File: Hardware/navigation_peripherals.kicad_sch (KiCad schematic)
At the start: 29 parts, among them J2 5-1814832-1, J3 Conn_01x04, J4 Conn_01x04, U10 BMP390, U11 W25N01GVZEIG_TR, U5 IST8310, U6 NEO-M8N, U7 BMI088, U8 TMP100, U9 24CW1280T-I/OT

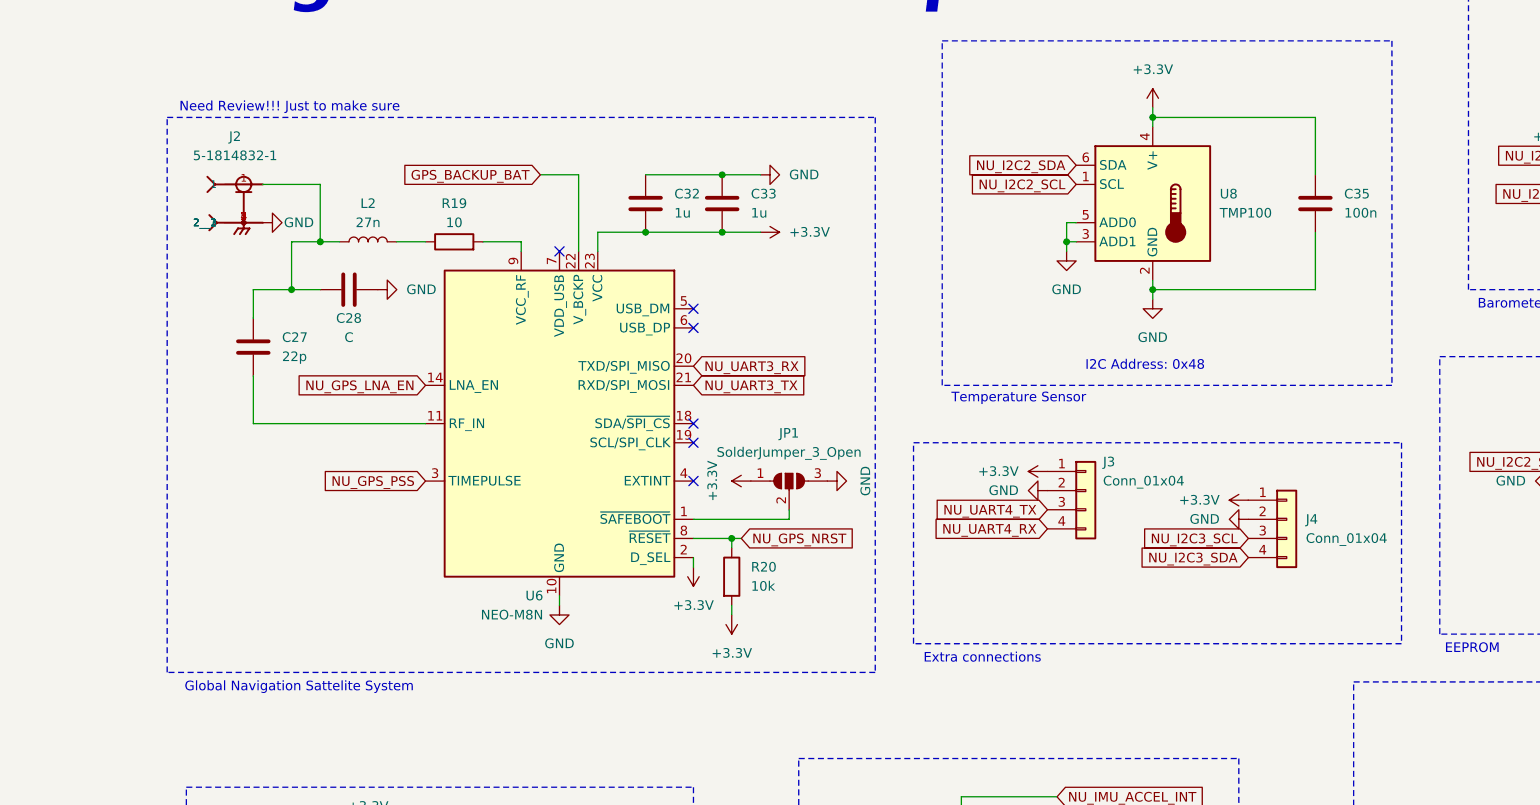
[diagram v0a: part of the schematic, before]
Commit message: hardware version 0.1.2, minor improvements and footprint selection (missing some gnss and bulk regulator components
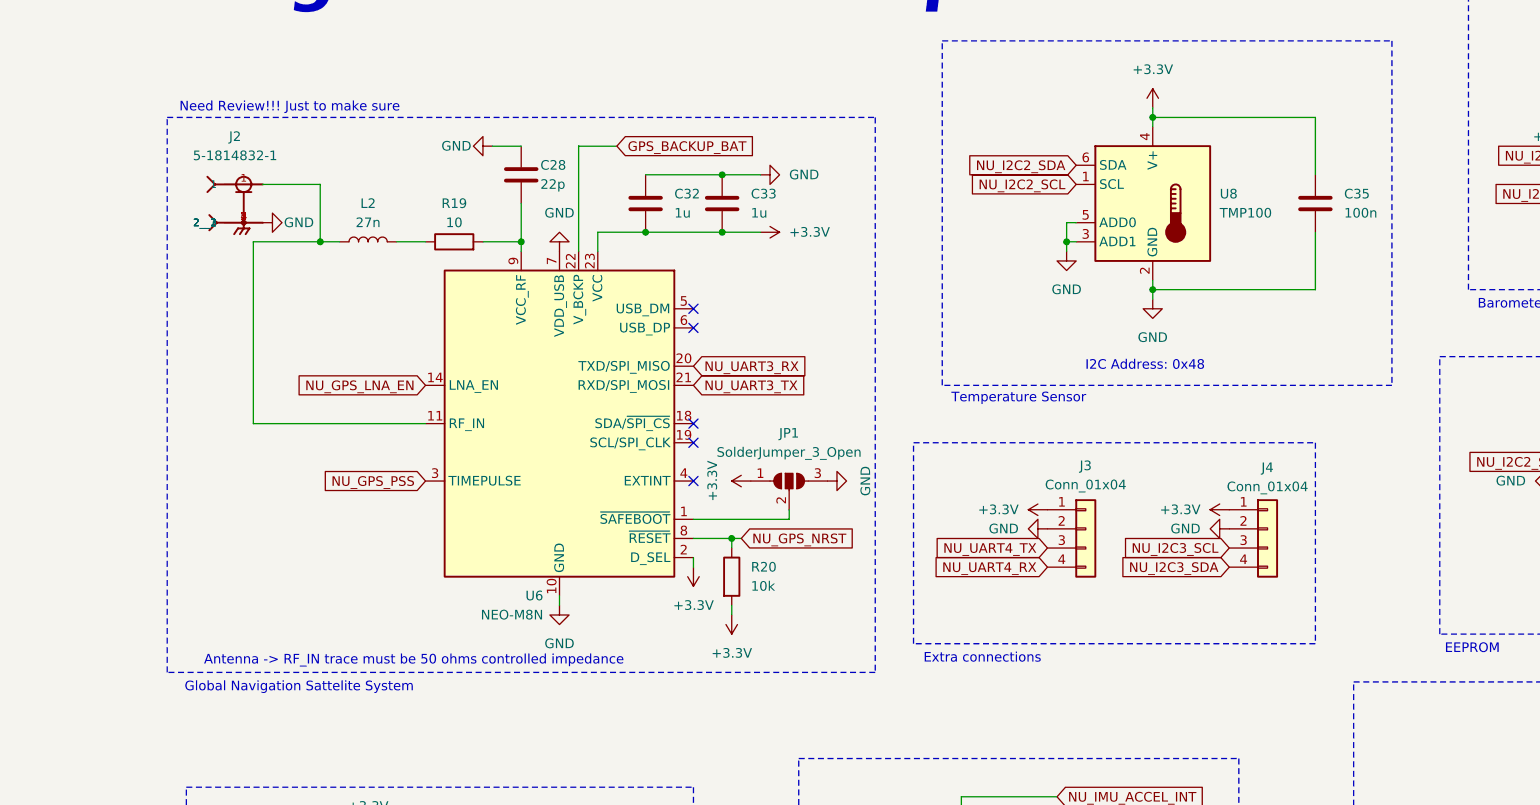
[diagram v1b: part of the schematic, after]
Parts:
- removed C27: 22p, symbol Device:C
- C28: value C -> 22p; footprint (none) -> Capacitor_SMD:C_0603_1608Metric
- C29, C32, C33: footprint (none) -> Capacitor_SMD:C_0805_2012Metric_Pad1.18x1.45mm_HandSolder
- J2: footprint 5-1814832-1:TE_5-1814832-1 -> Aircraft_Footprints:HIROSE_U.FL-R-SMT-1_80_
- J3, J4: footprint (none) -> Connector_JST:JST_PH_S4B-PH-K_1x04_P2.00mm_Horizontal
- JP1: footprint (none) -> Jumper:SolderJumper-3_P1.3mm_Open_RoundedPad1.0x1.5mm_NumberLabels
- R19, R20, R21, R22: footprint (none) -> Resistor_SMD:R_0603_1608Metric_Pad0.98x0.95mm_HandSolder
- U11: footprint W25N01GVZEIG_TR:SON127P800X600X80-9N -> Aircraft_Footprints:SON127P800X600X80-9N
- U6: footprint RF_GPS:ublox_NEO -> Aircraft_Footprints:XCVR_NEO-M8N-0
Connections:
- net GND: now also C28.1, U6.7 (VDD_USB); no longer C28.2
- net at J2.1, L2.1: now also U6.11 (RF_IN); no longer C28.1
- net at R19.2, U6.9 (VCC_RF): now also C28.2
- no-connect marks 9 -> 8
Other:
- note added: "Antenna -> RF_IN trace must be 50 ohms controlled impedance"
- moved on the sheet: J3, J4

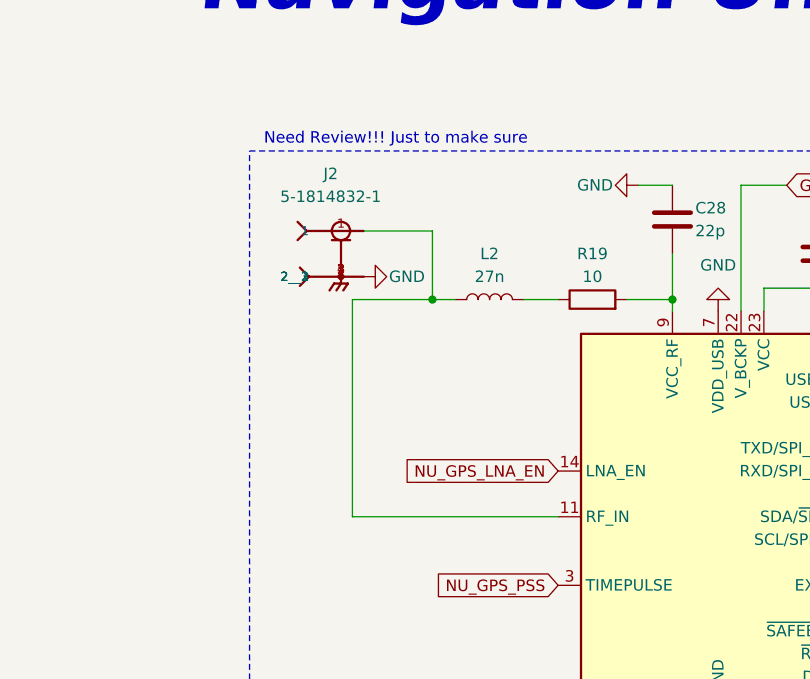
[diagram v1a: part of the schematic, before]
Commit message: board placement, no trails, just pain
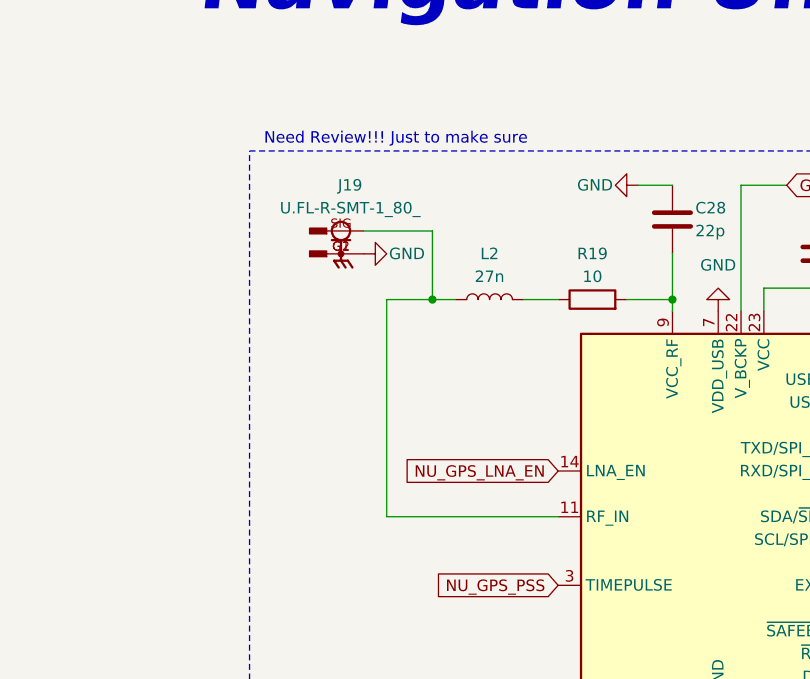
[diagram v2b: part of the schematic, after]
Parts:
- removed J2: 5-1814832-1, Aircraft_Footprints:HIROSE_U.FL-R-SMT-1_80_, symbol Aircraft_Components:5-1814832-1
- added J19: U.FL-R-SMT-1_80_, Aircraft_Footprints:HIROSE_U.FL-R-SMT-1_80_, symbol Aircraft_Components:U.FL-R-SMT-1_80_
- C28: Digikey_Link (none) -> https://www.digikey.com.br/pt/products/detail/kemet/C0603C2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; MPN (none) -> C0603C220J8GACTU
- C29: Digikey_Link (none) -> https://www.digikey.com.br/pt/products/detail/samsung-elect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; MPN (none) -> CL21B475KPFNNNE
- C30, C31, C34, C35, C36, C37, C38, C39: Digikey_Link (none) -> https://www.digikey.com.br/pt/products/detail/kemet/C0603C1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; MPN (none) -> C0603C104K8RACTU
- C32, C33: footprint Capacitor_SMD:C_0805_2012Metric_Pad1.18x1.45mm_HandSolder -> Capacitor_SMD:C_0603_1608Metric_Pad1.08x0.95mm_HandSolder; Digikey_Link (none) -> https://www.digikey.com.br/pt/products/detail/samsung-elect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; MPN (none) -> CL10B105KP8NNNC
- J3, J4: Digikey_Link (none) -> https://www.digikey.com.br/pt/products/detail/jst-sales-ame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; MPN (none) -> S4B-PH-K-S
- L2: footprint (none) -> Inductor_SMD:L_0603_1608Metric_Pad1.05x0.95mm_HandSolder; Digikey_Link (none) -> https://www.digikey.com.br/pt/products/detail/epcos-tdk-ele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; MPN (none) -> B82496C3270J000
- R19: Digikey_Link (none) -> https://www.digikey.com.br/pt/products/detail/stackpole-ele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; MPN (none) -> RMCF0603FT10R0
- R20, R21, R22: Digikey_Link (none) -> https://www.digikey.com.br/pt/products/detail/yageo/RC0603F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; MPN (none) -> RC0603FR-0710KL
- U10: Digikey_Link (none) -> https://www.digikey.com.br/pt/products/detail/bosch-sensort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; MPN (none) -> BMP390
- U11: Digikey_Link (none) -> https://www.digikey.com.br/pt/products/detail/winbond-elect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; MPN (none) -> W25N01GVZEIG-TR
- U5: Digikey_Link (none) -> https://www.digikey.com.br/pt/products/detail/isentek-inc/i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; MPN (none) -> IST8310
- U6: Digikey_Link (none) -> https://www.digikey.com.br/pt/products/detail/u-blox/neo-m8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; MPN (none) -> NEO-M8N-0
- U7: Digikey_Link (none) -> https://www.digikey.com.br/pt/products/detail/bosch-sensort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; MPN (none) -> BMI088
- U8: Digikey_Link (none) -> https://www.digikey.com.br/pt/products/detail/texas-instrum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; MPN (none) -> TMP100NA-3K
- U9: Digikey_Link (none) -> https://www.digikey.com.br/pt/products/detail/microchip-tec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; MPN (none) -> 24CW1280T-I/OT
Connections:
- net GND: now also J19.G1, J19.G2
- net at L2.1, U6.11 (RF_IN): now also J19.SIG
